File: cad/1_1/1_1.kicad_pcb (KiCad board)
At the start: 2 copper layers, 80 x 50 mm, 12 parts, among them J1 Conn_01x04_Pin, U1 ATtiny1616-M

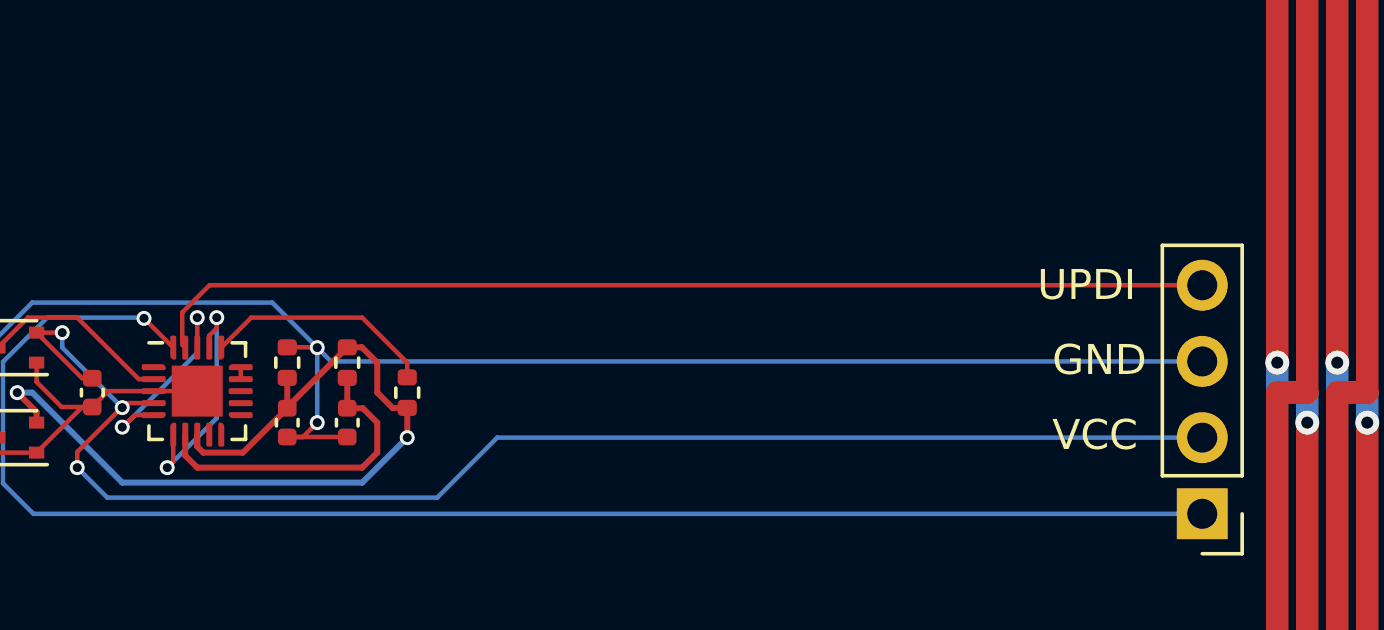
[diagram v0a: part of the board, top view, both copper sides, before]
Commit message: move UPDI wire to back
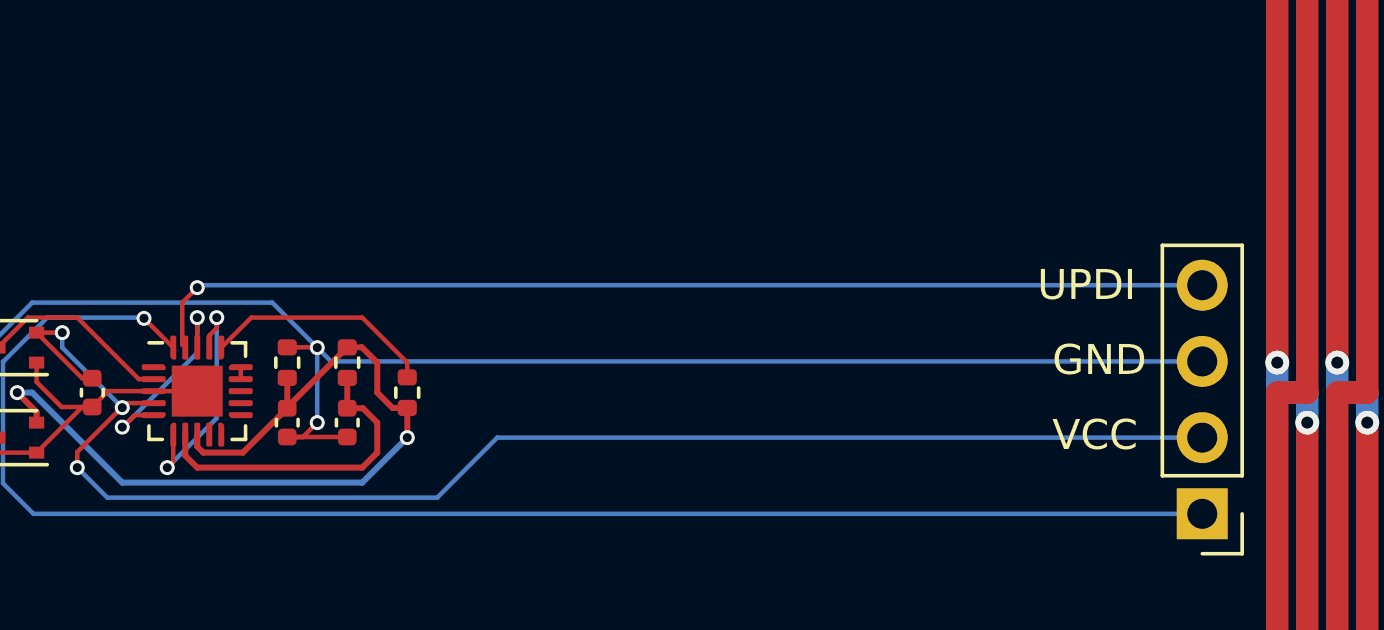
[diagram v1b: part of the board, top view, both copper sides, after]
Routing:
- net UPDI: track 35.6 -> 35.7 mm, vias 0 -> 1
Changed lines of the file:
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@@
 	)
 	(segment
-		(start 89.5 72.328248)
+		(start 89.6 73.5)
 		(end 89.5 73.4)
 		(width 0.15)
@@
 	)
 	(segment
-		(start 123.5 71.42)
-		(end 90.408248 71.42)
+		(start 89.5 73.4)
+		(end 89.5 72)
 		(width 0.15)
 		(layer "F.Cu")
@@
 	)
 	(segment
-		(start 89.5 73.4)
-		(end 89.6 73.5)
+		(start 89.5 72)
+		(end 90 71.5)
 		(width 0.15)
 		(layer "F.Cu")
 		(net 16)
 	)
-	(segment
-		(start 90.408248 71.42)
-		(end 89.5 72.328248)
-		(width 0.15)
-		(layer "F.Cu")
+	(via
+		(at 90 71.5)
+		(size 0.5)
+		(drill 0.3)
+		(layers "F.Cu" "B.Cu")
 		(net 16)
 	)
+	(segment
+		(start 123.5 71.42)
+		(end 90.08 71.42)
+		(width 0.15)
+		(layer "B.Cu")
+		(net 16)
+	)

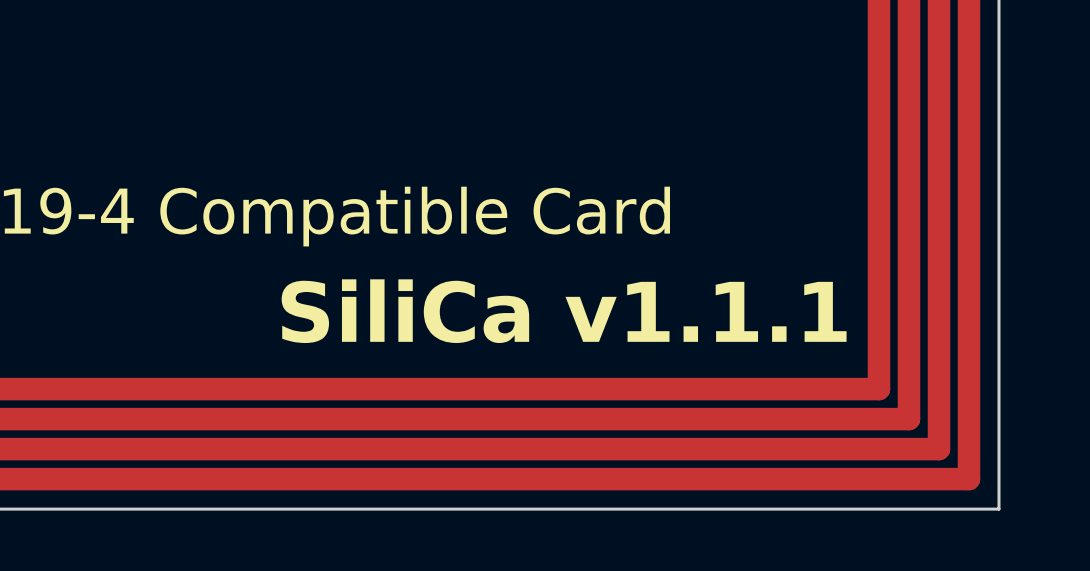
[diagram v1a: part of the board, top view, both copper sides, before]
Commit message: fix: update version number to 1.1.2 in PCB layout
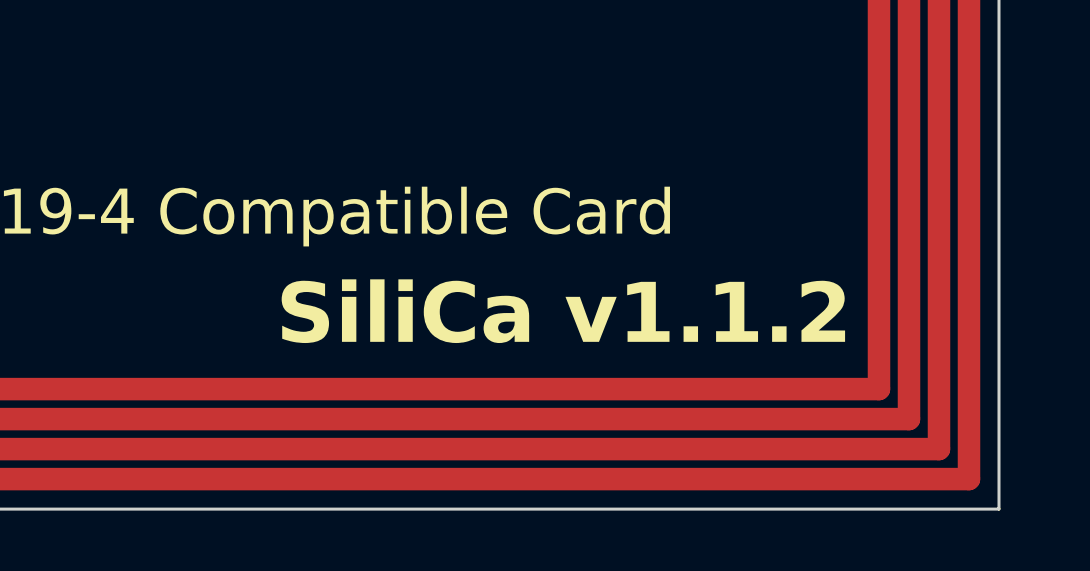
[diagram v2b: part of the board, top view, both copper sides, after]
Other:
- board text added: "SiliCa v1.1.2"
- board text removed: "SiliCa v1.1.1"
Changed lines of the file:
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@@
 		)
 	)
-	(gr_text "SiliCa v1.1.1"
+	(gr_text "SiliCa v1.1.2"
 		(at 115.5 93.5 0)
 		(layer "F.SilkS")

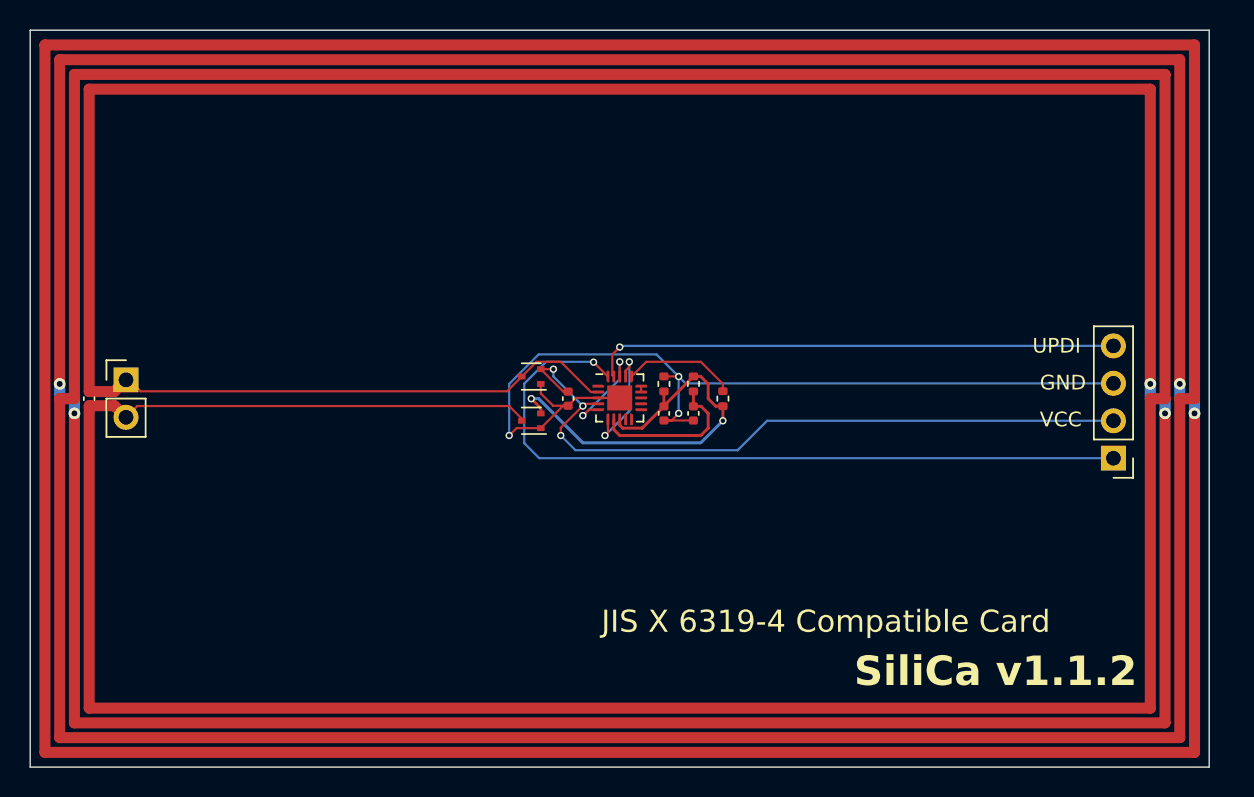
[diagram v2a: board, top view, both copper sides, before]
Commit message: add tooling holes
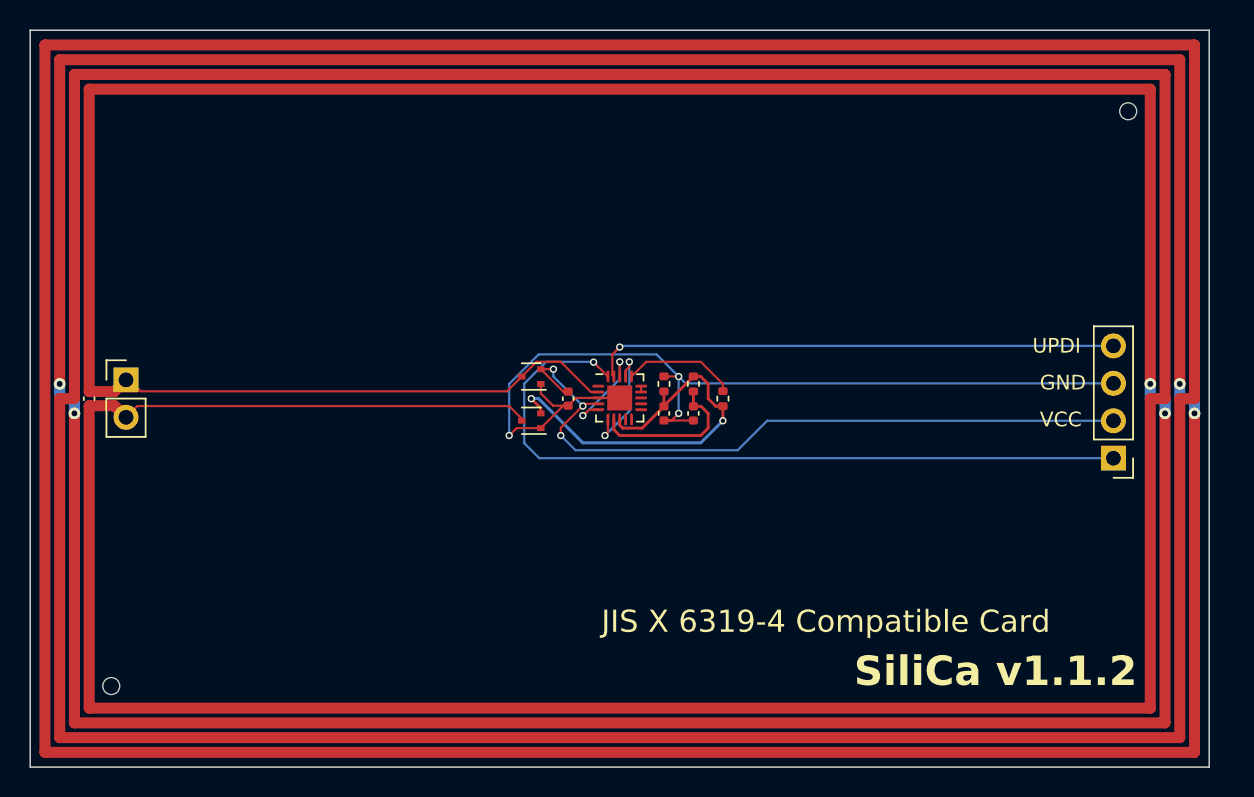
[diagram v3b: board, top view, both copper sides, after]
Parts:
- added REF**: ToolingHole_1.152mm, MountingHole:ToolingHole_1.152mm, F.Cu at (124.5, 55.5)
- added REF**: ToolingHole_1.152mm, MountingHole:ToolingHole_1.152mm, F.Cu at (55.5, 94.5)
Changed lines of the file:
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@@
 	(net 16 "UPDI")
 	(net 17 "TxD")
+	(footprint "MountingHole:ToolingHole_1.152mm"
+		(layer "F.Cu")
+		(at 124.5 55.5)
+		(descr "Tooling Hole 1.152mm, 1.3mm solder mask, JLCPCB specification, https://jlcpcb.com/help/article/How-to-add-tooling-holes-for-PCB-assembly-order")
+		(tags "mounting")
+		(property "Reference" "REF**"
+			(at 0 -1.5 0)
+			(layer "F.SilkS")
+			(hide yes)
+			(effects
+				(font
+					(size 1 1)
+					(thickness 0.15)
+				)
+			)
+		)
+		(property "Value" "ToolingHole_1.152mm"
+			(at 0 1.6 0)
+			(layer "F.Fab")
+			(effects
+				(font
+					(size 1 1)
+					(thickness 0.15)
+				)
+			)
+		)
+		(property "Datasheet" ""
+			(at 0 0 0)
+			(unlocked yes)
+			(layer "F.Fab")
+			(hide yes)
+			(effects
+				(font
+					(size 1.27 1.27)
+					(thickness 0.15)
+				)
+			)
+		)
+		(property "Description" ""
+			(at 0 0 0)
+			(unlocked yes)
+			(layer "F.Fab")
+			(hide yes)
+			(effects
+				(font
+					(size 1.27 1.27)
+					(thickness 0.15)
+				)
+			)
+		)
+		(attr exclude_from_pos_files exclude_from_bom)
+		(fp_circle
+			(center 0 0)
+			(end 0.7 0)
+			(stroke
+				(width 0.05)
+				(type solid)
+			)
+			(fill no)
+			(layer "F.CrtYd")
+		)
+		(fp_text user "${REFERENCE}"
+			(at 0 0 0)
+			(layer "F.Fab")
+			(effects
+				(font
+					(size 1 1)
+					(thickness 0.15)
+				)
+			)
+		)
+		(pad "" np_thru_hole circle
+			(at 0 0)
+			(size 1.152 1.152)
+			(drill 1.152)
+			(layers "*.Cu" "*.Mask")
+			(solder_mask_margin 0.074)
+		)
+		(zone
+			(net 0)
+			(net_name "")
+			(layers "F.Cu" "B.Cu")
+			(hatch edge 0.5)
+			(connect_pads
+				(clearance 0)
+			)
+			(min_thickness 0.25)
+			(filled_areas_thickness no)
+			(keepout
+				(tracks not_allowed)
+				(vias allowed)
+				(pads allowed)
+				(copperpour not_allowed)
+				(footprints not_allowed)
+			)
+			(placement
+				(enabled no)
+				(sheetname "")
+			)
+			(fill
+				(thermal_gap 0.5)
+				(thermal_bridge_width 0.5)
+			)
+			(polygon
+				(pts
+					(xy 125.2 55.5) (xy 125.179659 55.332479) (xy 125.119819 55.174694) (xy 125.023958 55.035814) (xy 124.897645 54.923911)
+					(xy 124.748223 54.845489) (xy 124.584376 54.805104) (xy 124.415624 54.805104) (xy 124.251777 54.845489)
+					(xy 124.102355 54.923911) (xy 123.976042 55.035814) (xy 123.880181 55.174694) (xy 123.820341 55.332479)
+					(xy 123.8 55.5) (xy 123.820341 55.667521) (xy 123.880181 55.825306) (xy 123.976042 55.964186) (xy 124.102355 56.076089)
+					(xy 124.251777 56.154511) (xy 124.415624 56.194896) (xy 124.584376 56.194896) (xy 124.748223 56.154511)
+					(xy 124.897645 56.076089) (xy 125.023958 55.964186) (xy 125.119819 55.825306) (xy 125.179659 55.667521)
+				)
+			)
+		)
+		(embedded_fonts no)
+	)
 	(footprint "Package_TO_SOT_SMD:SOT-523"
 		(layer "F.Cu")
@@
 		)
 	)
+	(footprint "MountingHole:ToolingHole_1.152mm"
+		(layer "F.Cu")
+		(at 55.5 94.5)
+		(descr "Tooling Hole 1.152mm, 1.3mm solder mask, JLCPCB specification, https://jlcpcb.com/help/article/How-to-add-tooling-holes-for-PCB-assembly-order")
+		(tags "mounting")
+		(property "Reference" "REF**"
+			(at 0 -1.5 0)
+			(layer "F.SilkS")
+			(hide yes)
+			(effects
+				(font
+					(size 1 1)
+					(thickness 0.15)
+				)
+			)
+		)
+		(property "Value" "ToolingHole_1.152mm"
+			(at 0 1.6 0)
+			(layer "F.Fab")
+			(effects
+				(font
+					(size 1 1)
+					(thickness 0.15)
+				)
+			)
+		)
+		(property "Datasheet" ""
+			(at 0 0 0)
+			(unlocked yes)
+			(layer "F.Fab")
+			(hide yes)
+			(effects
+				(font
+					(size 1.27 1.27)
+					(thickness 0.15)
+				)
+			)
+		)
+		(property "Description" ""
+			(at 0 0 0)
+			(unlocked yes)
+			(layer "F.Fab")
+			(hide yes)
+			(effects
+				(font
+					(size 1.27 1.27)
+					(thickness 0.15)
+				)
+			)
+		)
+		(attr exclude_from_pos_files exclude_from_bom)
+		(fp_circle
+			(center 0 0)
+			(end 0.7 0)
+			(stroke
+				(width 0.05)
+				(type solid)
+			)
+			(fill no)
+			(layer "F.CrtYd")
+		)
+		(fp_text user "${REFERENCE}"
+			(at 0 0 0)
+			(layer "F.Fab")
+			(effects
+				(font
+					(size 1 1)
+					(thickness 0.15)
+				)
+			)
+		)
+		(pad "" np_thru_hole circle
+			(at 0 0)
+			(size 1.152 1.152)
+			(drill 1.152)
+			(layers "*.Cu" "*.Mask")
+			(solder_mask_margin 0.074)
+		)
+		(zone
+			(net 0)
+			(net_name "")
+			(layers "F.Cu" "B.Cu")
+			(hatch edge 0.5)
+			(connect_pads
+				(clearance 0)
+			)
+			(min_thickness 0.25)
+			(filled_areas_thickness no)
+			(keepout
+				(tracks not_allowed)
+				(vias allowed)
+				(pads allowed)
+				(copperpour not_allowed)
+				(footprints not_allowed)
+			)
+			(placement
+				(enabled no)
+				(sheetname "")
+			)
+			(fill
+				(thermal_gap 0.5)
+				(thermal_bridge_width 0.5)
+			)
+			(polygon
+				(pts
+					(xy 56.2 94.5) (xy 56.179659 94.332479) (xy 56.119819 94.174694) (xy 56.023958 94.035814) (xy 55.897645 93.923911)
+					(xy 55.748223 93.845489) (xy 55.584376 93.805104) (xy 55.415624 93.805104) (xy 55.251777 93.845489)
+					(xy 55.102355 93.923911) (xy 54.976042 94.035814) (xy 54.880181 94.174694) (xy 54.820341 94.332479)
+					(xy 54.8 94.5) (xy 54.820341 94.667521) (xy 54.880181 94.825306) (xy 54.976042 94.964186) (xy 55.102355 95.076089)
+					(xy 55.251777 95.154511) (xy 55.415624 95.194896) (xy 55.584376 95.194896) (xy 55.748223 95.154511)
+					(xy 55.897645 95.076089) (xy 56.023958 94.964186) (xy 56.119819 94.825306) (xy 56.179659 94.667521)
+				)
+			)
+		)
+		(embedded_fonts no)
+	)
 	(footprint "Capacitor_SMD:C_0402_1005Metric"

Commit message: move tooling holes
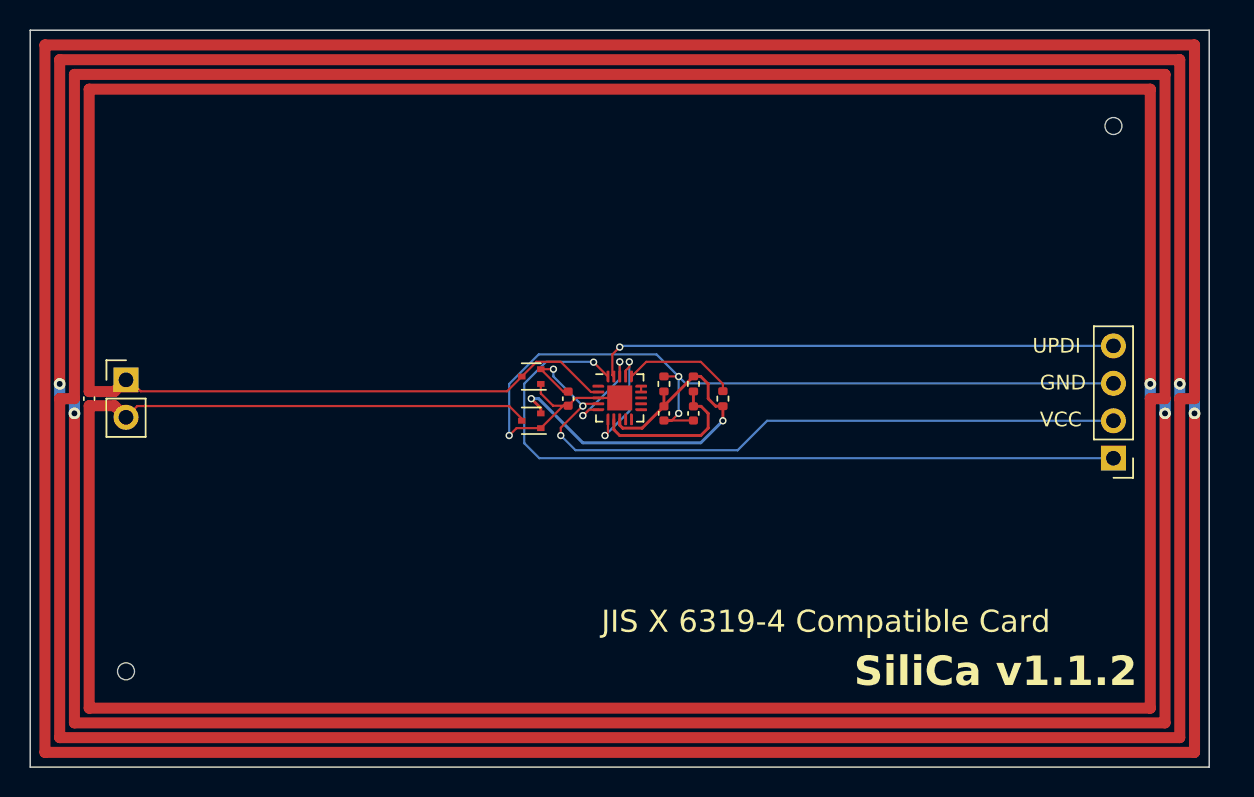
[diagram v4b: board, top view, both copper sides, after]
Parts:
- moved REF** 1.41 mm to (123.5, 56.5)
- moved REF** 1.41 mm to (56.5, 93.5)
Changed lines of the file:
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@@
 	(footprint "MountingHole:ToolingHole_1.152mm"
 		(layer "F.Cu")
-		(at 124.5 55.5)
+		(at 123.5 56.5)
 		(descr "Tooling Hole 1.152mm, 1.3mm solder mask, JLCPCB specification, https://jlcpcb.com/help/article/How-to-add-tooling-holes-for-PCB-assembly-order")
 		(tags "mounting")
@@
 			(polygon
 				(pts
-					(xy 125.2 55.5) (xy 125.179659 55.332479) (xy 125.119819 55.174694) (xy 125.023958 55.035814) (xy 124.897645 54.923911)
-					(xy 124.748223 54.845489) (xy 124.584376 54.805104) (xy 124.415624 54.805104) (xy 124.251777 54.845489)
-					(xy 124.102355 54.923911) (xy 123.976042 55.035814) (xy 123.880181 55.174694) (xy 123.820341 55.332479)
-					(xy 123.8 55.5) (xy 123.820341 55.667521) (xy 123.880181 55.825306) (xy 123.976042 55.964186) (xy 124.102355 56.076089)
-					(xy 124.251777 56.154511) (xy 124.415624 56.194896) (xy 124.584376 56.194896) (xy 124.748223 56.154511)
-					(xy 124.897645 56.076089) (xy 125.023958 55.964186) (xy 125.119819 55.825306) (xy 125.179659 55.667521)
+					(xy 124.2 56.5) (xy 124.179659 56.332479) (xy 124.119819 56.174694) (xy 124.023958 56.035814) (xy 123.897645 55.923911)
+					(xy 123.748223 55.845489) (xy 123.584376 55.805104) (xy 123.415624 55.805104) (xy 123.251777 55.845489)
+					(xy 123.102355 55.923911) (xy 122.976042 56.035814) (xy 122.880181 56.174694) (xy 122.820341 56.332479)
+					(xy 122.8 56.5) (xy 122.820341 56.667521) (xy 122.880181 56.825306) (xy 122.976042 56.964186) (xy 123.102355 57.076089)
+					(xy 123.251777 57.154511) (xy 123.415624 57.194896) (xy 123.584376 57.194896) (xy 123.748223 57.154511)
+					(xy 123.897645 57.076089) (xy 124.023958 56.964186) (xy 124.119819 56.825306) (xy 124.179659 56.667521)
 				)
 			)
@@
 	(footprint "MountingHole:ToolingHole_1.152mm"
 		(layer "F.Cu")
-		(at 55.5 94.5)
+		(at 56.5 93.5)
 		(descr "Tooling Hole 1.152mm, 1.3mm solder mask, JLCPCB specification, https://jlcpcb.com/help/article/How-to-add-tooling-holes-for-PCB-assembly-order")
 		(tags "mounting")
@@
 			(polygon
 				(pts
-					(xy 56.2 94.5) (xy 56.179659 94.332479) (xy 56.119819 94.174694) (xy 56.023958 94.035814) (xy 55.897645 93.923911)
-					(xy 55.748223 93.845489) (xy 55.584376 93.805104) (xy 55.415624 93.805104) (xy 55.251777 93.845489)
-					(xy 55.102355 93.923911) (xy 54.976042 94.035814) (xy 54.880181 94.174694) (xy 54.820341 94.332479)
-					(xy 54.8 94.5) (xy 54.820341 94.667521) (xy 54.880181 94.825306) (xy 54.976042 94.964186) (xy 55.102355 95.076089)
-					(xy 55.251777 95.154511) (xy 55.415624 95.194896) (xy 55.584376 95.194896) (xy 55.748223 95.154511)
-					(xy 55.897645 95.076089) (xy 56.023958 94.964186) (xy 56.119819 94.825306) (xy 56.179659 94.667521)
-				)
-			)
+					(xy 57.2 93.5) (xy 57.179659 93.332479) (xy 57.119819 93.174694) (xy 57.023958 93.035814) (xy 56.897645 92.923911)
+					(xy 56.748223 92.845489) (xy 56.584376 92.805104) (xy 56.415624 92.805104) (xy 56.251777 92.845489)
+					(xy 56.102355 92.923911) (xy 55.976042 93.035814) (xy 55.880181 93.174694) (xy 55.820341 93.332479)
+					(xy 55.8 93.5) (xy 55.820341 93.667521) (xy 55.880181 93.825306) (xy 55.976042 93.964186) (xy 56.102355 94.076089)
+					(xy 56.251777 94.154511) (xy 56.415624 94.194896) (xy 56.584376 94.194896) (xy 56.748223 94.154511)
+					(xy 56.897645 94.076089) (xy 57.023958 93.964186) (xy 57.119819 93.825306) (xy 57.179659 93.667521)
+				)
+			)
